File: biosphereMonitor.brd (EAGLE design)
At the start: 85 x 85 mm, 62 parts, among them IC1 XMEGA32A4AU, IC2 LM35, IC3 FT232RL, IC4 NE555D, IC5 SST25VF040, Q1 16Mhz, Q2 32kHz

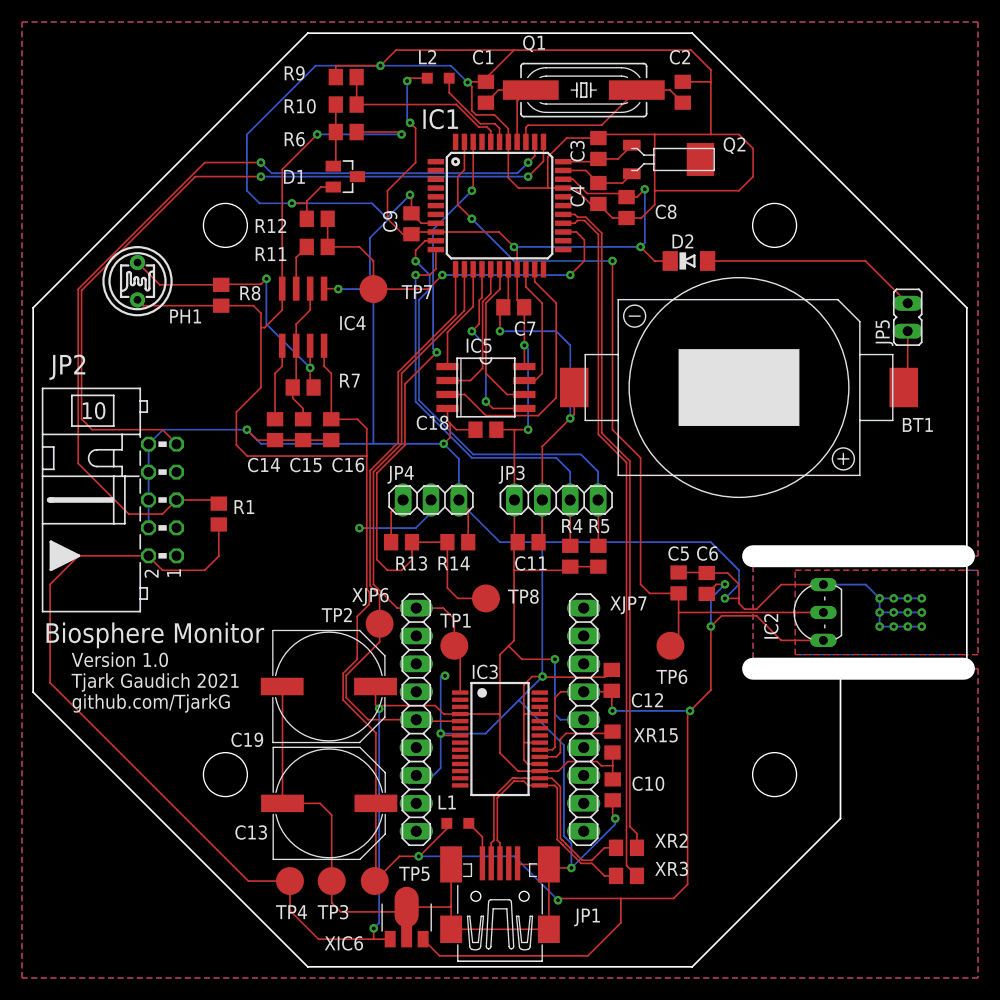
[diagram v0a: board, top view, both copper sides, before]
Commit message: changed rx with tx
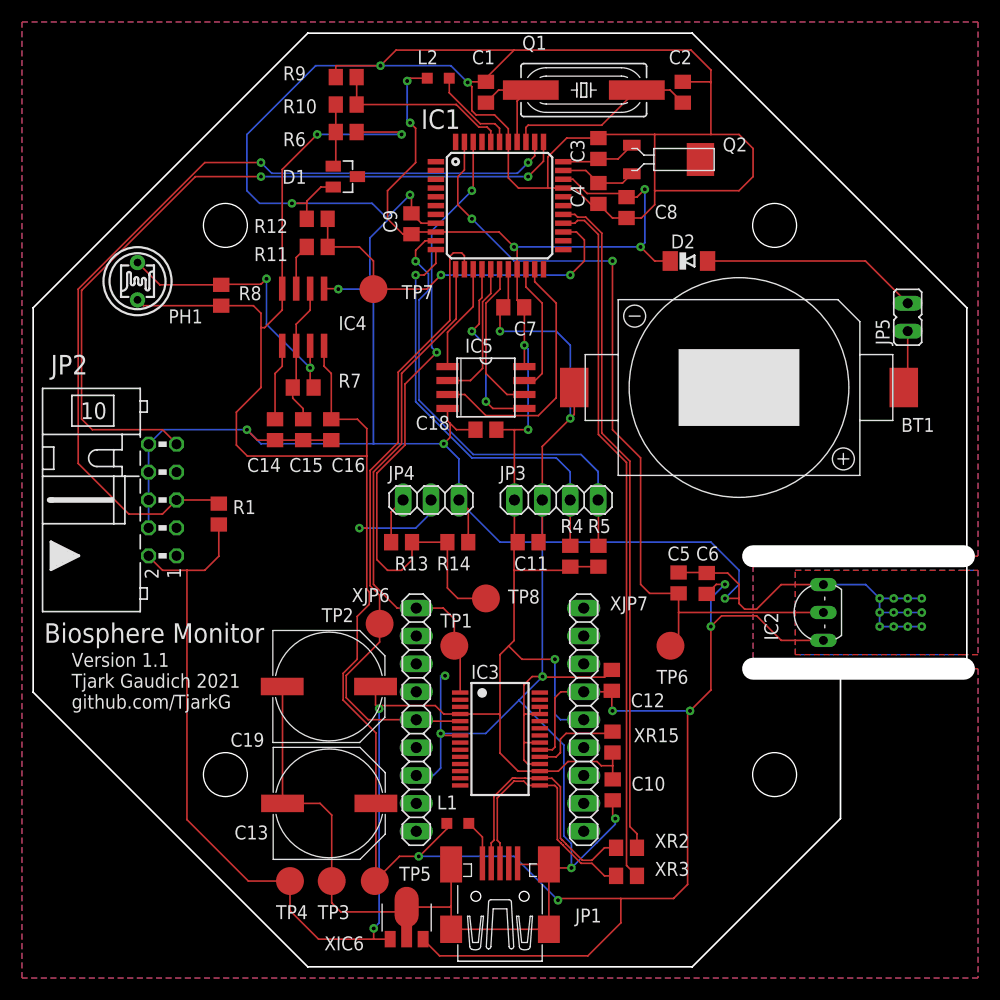
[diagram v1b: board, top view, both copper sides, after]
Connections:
- net USB_RX: now also IC1.13; no longer IC1.12
- net USB_TX: now also IC1.12; no longer IC1.13
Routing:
- net +3V3: track 250.1 -> 236.2 mm
- net USB_RX: track 55.1 -> 58.9 mm
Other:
- board text added: "Version 1.1 Tjark Gaudich 2021 github.com/TjarkG"
- board text removed: "Version 1.0 Tjark Gaudich 2021 github.com/TjarkG"
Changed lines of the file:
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@@
 <wire x1="42.24" y1="-5.12" x2="23.04" y2="-5.12" width="2" layer="46"/>
 <wire x1="-17.5" y1="42.5" x2="17.5" y2="42.5" width="0.1524" layer="20"/>
-<text x="-39" y="-19" size="1.27" layer="25">Version 1.0
+<text x="-39" y="-19" size="1.27" layer="25">Version 1.1
 Tjark Gaudich 2021
 github.com/TjarkG</text>
@@
 <wire x1="-31.99" y1="-5.08" x2="-31.99" y2="-5.13" width="0.1524" layer="1"/>
 <wire x1="-31.99" y1="-5.13" x2="-30.72" y2="-6.4" width="0.1524" layer="1"/>
-<wire x1="-30.72" y1="-6.4" x2="-26.88" y2="-6.4" width="0.1524" layer="1"/>
+<wire x1="-30.72" y1="-6.4" x2="-28.5" y2="-6.4" width="0.1524" layer="1"/>
+<wire x1="-28.5" y1="-6.4" x2="-26.88" y2="-6.4" width="0.1524" layer="1"/>
 <wire x1="-26.88" y1="-6.4" x2="-25.6" y2="-5.12" width="0.1524" layer="1"/>
 <wire x1="-25.6" y1="-5.12" x2="-25.6" y2="-2.23" width="0.1524" layer="1"/>
@@
 <wire x1="3.625" y1="-24.685" x2="1.645" y2="-24.685" width="0.1524" layer="1"/>
 <wire x1="1.645" y1="-24.685" x2="0" y2="-23.04" width="0.1524" layer="1"/>
-<wire x1="-31.99" y1="-5.08" x2="-38.36" y2="-5.08" width="0.1524" layer="1"/>
-<wire x1="-38.36" y1="-5.08" x2="-40.96" y2="-7.68" width="0.1524" layer="1"/>
-<wire x1="-40.96" y1="-7.68" x2="-40.96" y2="-16.64" width="0.1524" layer="1"/>
-<wire x1="-22.91" y1="-34.69" x2="-19.12" y2="-34.69" width="0.1524" layer="1"/>
-<wire x1="-40.96" y1="-16.64" x2="-22.91" y2="-34.69" width="0.1524" layer="1"/>
+<wire x1="-19.12" y1="-34.69" x2="-22.91" y2="-34.69" width="0.1524" layer="1"/>
 <wire x1="1.31" y1="0" x2="1.31" y2="-3.54" width="0.1524" layer="1"/>
 <wire x1="1.31" y1="-3.54" x2="1.61" y2="-3.84" width="0.1524" layer="1"/>
@@
 <via x="-11.5" y="-39" extent="1-16" drill="0.35"/>
 <wire x1="-11.5" y1="-39" x2="-11.5" y2="-39.981" width="0.1524" layer="1"/>
+<wire x1="-22.91" y1="-34.69" x2="-28.5" y2="-29.1" width="0.1524" layer="1"/>
+<wire x1="-28.5" y1="-29.1" x2="-28.5" y2="-6.4" width="0.1524" layer="1"/>
 </signal>
 <signal name="GND">
@@
 </signal>
 <signal name="USB_RX">
-<contactref element="IC1" pad="12"/>
 <contactref element="TP2" pad="TP"/>
 <contactref element="IC3" pad="5"/>
@@
 <wire x1="-10.96" y1="-8.67105625" x2="-11.8248" y2="-7.80625625" width="0.1524" layer="1"/>
 <wire x1="-9.2648" y1="5.24625625" x2="-9.2648" y2="11.64625625" width="0.1524" layer="1"/>
-<wire x1="-4.04" y1="16.87105625" x2="-4.04" y2="21" width="0.1524" layer="1"/>
 <wire x1="-11.8248" y1="-7.80625625" x2="-11.8248" y2="2.68625625" width="0.1524" layer="1"/>
 <wire x1="-11.8248" y1="2.68625625" x2="-9.2648" y2="5.24625625" width="0.1524" layer="1"/>
-<wire x1="-9.2648" y1="11.64625625" x2="-4.04" y2="16.87105625" width="0.1524" layer="1"/>
 <contactref element="XJP6" pad="5"/>
 <wire x1="-3.625" y1="-20.135" x2="-7.485" y2="-20.135" width="0.1524" layer="1"/>
@@
 <wire x1="-10.96" y1="-12.934" x2="-14" y2="-15.974" width="0.1524" layer="1"/>
 <wire x1="-10.96" y1="-12.934" x2="-10.96" y2="-11.27" width="0.1524" layer="1"/>
+<contactref element="IC1" pad="13"/>
+<wire x1="-4.5662" y1="22.1778" x2="-4.244" y2="22.5" width="0.1524" layer="1"/>
+<wire x1="-4.244" y1="22.5" x2="-3.5" y2="22.5" width="0.1524" layer="1"/>
+<wire x1="-3.5" y1="22.5" x2="-3.24" y2="22.24" width="0.1524" layer="1"/>
+<wire x1="-3.24" y1="22.24" x2="-3.24" y2="21" width="0.1524" layer="1"/>
+<wire x1="-9.2648" y1="11.64625625" x2="-4.5662" y2="16.34485625" width="0.1524" layer="1"/>
+<wire x1="-4.5662" y1="16.34485625" x2="-4.5662" y2="22.1778" width="0.1524" layer="1"/>
 </signal>
 <signal name="USB_TX">
-<contactref element="IC1" pad="13"/>
 <contactref element="TP1" pad="TP"/>
 <contactref element="IC3" pad="1"/>
-<wire x1="-3.24" y1="21" x2="-3.24" y2="17.24" width="0.1524" layer="1"/>
 <wire x1="-8.96" y1="11.52" x2="-8.96" y2="5.12" width="0.1524" layer="1"/>
 <wire x1="-8.96" y1="5.12" x2="-11.52" y2="2.56" width="0.1524" layer="1"/>
 <wire x1="-11.52" y1="2.56" x2="-11.52" y2="-7.68" width="0.1524" layer="1"/>
 <wire x1="-11.52" y1="-7.68" x2="-9.36" y2="-9.84" width="0.1524" layer="1"/>
-<wire x1="-3.24" y1="17.24" x2="-8.96" y2="11.52" width="0.1524" layer="1"/>
 <contactref element="XJP6" pad="1"/>
+<wire x1="-3.99" y1="16.49" x2="-8.96" y2="11.52" width="0.1524" layer="1"/>
 <wire x1="-3.625" y1="-17.535" x2="-3.625" y2="-13.805" width="0.1524" layer="1"/>
 <wire x1="-3.625" y1="-13.805" x2="-4.16" y2="-13.27" width="0.1524" layer="1"/>
@@
 <wire x1="-4.16" y1="-10.84" x2="-4.16" y2="-13.27" width="0.1524" layer="1"/>
 <wire x1="-5.16" y1="-9.84" x2="-4.16" y2="-10.84" width="0.1524" layer="1"/>
+<contactref element="IC1" pad="12"/>
+<wire x1="-4.04" y1="21" x2="-3.99" y2="20.95" width="0.1524" layer="1"/>
+<wire x1="-3.99" y1="20.95" x2="-3.99" y2="16.49" width="0.1524" layer="1"/>
 </signal>
 <signal name="AVCC">
@@
 <wire x1="8.96" y1="-0.03" x2="8.93" y2="0" width="0.1524" layer="1"/>
 <wire x1="8.93" y1="0" x2="8.93" y2="2.59" width="0.1524" layer="16"/>
-<wire x1="-7.3752" y1="18.2248" x2="-6.4" y2="19.2" width="0.1524" layer="16"/>
-<wire x1="-6.4" y1="19.2" x2="-6.4" y2="20.48" width="0.1524" layer="16"/>
+<wire x1="-7.3752" y1="18.2248" x2="-6.516" y2="19.084" width="0.1524" layer="16"/>
+<wire x1="-6.516" y1="19.084" x2="-6.516" y2="20.596" width="0.1524" layer="16"/>
 <wire x1="-7.68" y1="21.7354" x2="-7.6554" y2="21.7354" width="0.1524" layer="16"/>
-<wire x1="-6.4" y1="20.48" x2="-7.6554" y2="21.7354" width="0.1524" layer="16"/>
+<wire x1="-6.516" y1="20.596" x2="-7.6554" y2="21.7354" width="0.1524" layer="16"/>
 <via x="-7.68" y="21.7354" extent="1-16" drill="0.35"/>
 <wire x1="-6.8047125" y1="23.6" x2="-7.68" y2="22.7247125" width="0.1524" layer="1"/>
@@
 <wire x1="-7.68" y1="8.96" x2="-7.68" y2="20.48" width="0.1524" layer="16"/>
 <via x="-7.68" y="20.48" extent="1-16" drill="0.35"/>
-<wire x1="-7.68" y1="20.48" x2="-6.4" y2="20.48" width="0.1524" layer="1"/>
-<wire x1="-6.4" y1="20.48" x2="-5.84" y2="21.04" width="0.1524" layer="1"/>
-<wire x1="-5.84" y1="21.04" x2="-5.84" y2="22.8" width="0.1524" layer="1"/>
+<wire x1="-7.68" y1="20.48" x2="-6.9" y2="20.48" width="0.1524" layer="1"/>
+<wire x1="-6.9" y1="20.48" x2="-5.84" y2="21.54" width="0.1524" layer="1"/>
+<wire x1="-5.84" y1="21.54" x2="-5.84" y2="22.8" width="0.1524" layer="1"/>
 </signal>
 <signal name="LIGHT">
@@
 <wire x1="-11.52" y1="21.76" x2="-12.8" y2="23.04" width="0.1524" layer="1"/>
 <wire x1="-12.8" y1="23.04" x2="-15.69" y2="23.04" width="0.1524" layer="1"/>
-<wire x1="-11.52" y1="19.2" x2="-6.528" y2="19.2" width="0.1524" layer="1"/>
-<wire x1="-6.528" y1="19.2" x2="-5.248" y2="20.48" width="0.1524" layer="1"/>
-<via x="-5.248" y="20.48" extent="1-16" drill="0.35"/>
-<wire x1="-5.248" y1="20.48" x2="6.4" y2="20.48" width="0.1524" layer="16"/>
+<wire x1="-11.52" y1="19.2" x2="-6.656" y2="19.2" width="0.1524" layer="1"/>
+<wire x1="-6.656" y1="19.2" x2="-5.376" y2="20.48" width="0.1524" layer="1"/>
+<via x="-5.376" y="20.48" extent="1-16" drill="0.35"/>
+<wire x1="-5.376" y1="20.48" x2="6.4" y2="20.48" width="0.1524" layer="16"/>
 <via x="6.4" y="20.48" extent="1-16" drill="0.35"/>
 <wire x1="6.4" y1="20.48" x2="7.68" y2="21.76" width="0.1524" layer="1"/>
@@
 <via x="-5.76" y="13.44" extent="1-16" drill="0.35"/>
 <via x="-2.56" y="28.16" extent="1-16" drill="0.35"/>
-<wire x1="-6.0952" y1="24.6248" x2="-6.0952" y2="13.7752" width="0.1524" layer="16"/>
-<wire x1="-5.76" y1="13.44" x2="-6.0952" y2="13.7752" width="0.1524" layer="16"/>
-<wire x1="-6.0952" y1="24.6248" x2="-2.56" y2="28.16" width="0.1524" layer="16"/>
+<wire x1="-6.2232" y1="24.4968" x2="-6.2232" y2="13.9032" width="0.1524" layer="16"/>
+<wire x1="-5.76" y1="13.44" x2="-6.2232" y2="13.9032" width="0.1524" layer="16"/>
+<wire x1="-6.2232" y1="24.4968" x2="-2.56" y2="28.16" width="0.1524" layer="16"/>
 <wire x1="-2.56" y1="28.16" x2="-2.44" y2="28.28" width="0.1524" layer="1"/>
 <wire x1="-2.44" y1="28.28" x2="-2.44" y2="32.6" width="0.1524" layer="1"/>
